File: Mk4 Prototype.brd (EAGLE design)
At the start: 6 parts

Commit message: Initial shape and some layout ideas
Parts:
- added ARTWORK1: ARTWORK_JOYSTICK, TiLDA Mk4 Parts:TILDA_ARTWORK_JOYSTICK
- added ARTWORK2: ARTWORK_KEYPAD, TiLDA Mk4 Parts:TILDA_ARTWORK_KEYPAD
- added C1: 0603 1u/10V/X5R, TiLDA Mk4 Parts:C0603K-SMALL
- added C38: 0603 4u7/10V/X5R, TiLDA Mk4 Parts:C0603K-SMALL
- added C45: 0603 100n/10V/X5R, TiLDA Mk4 Parts:C0603K-SMALL
- added IC1: MSP432E401, TiLDA Mk4 Parts:QFP128-0.4
- added IC2: AS4C8M16SA-7TCN, TiLDA Mk4 Parts:TSOP54-400
- added IC3: CC3120MOD, TiLDA Mk4 Parts:CC3100MOD-LWK
- added IC5: SIM800C, TiLDA Mk4 Parts:SIM800C
- added J2: ER-CON50HT-1, TiLDA Mk4 Parts:FH12-50S-0.5SH
- added J3: 2x5 1.27mm (NP), TiLDA Mk4 Parts:PINHEAD_2X05_127
- added JP1: (no value), TiLDA Mk4 Parts:JST-2-SMD
- added JP2: 1x03, TiLDA Mk4 Parts:1X03_LOCK
- added JP4: (NP), TiLDA Mk4 Parts:TC2030-MCP-NL
- added LAYERS1: LAYER_NUMBRS_4_SMALL, TiLDA Mk4 Parts:LAYER_NUMBERS_4_SMALL
- added LED1, LED2: (no value), TiLDA Mk4 Parts:WS2812B
- added OUTLINE1: TILDA_MK3_BOARDOUTLINE-MK4, TiLDA Mk4 Parts:TILDA_MK4_OUTLINE
- added Q8: CSD13202Q2, TiLDA Mk4 Parts:Q2
- added R44, R47, R48, R49: 0603 12R/5%, TiLDA Mk4 Parts:C0603K-SMALL
- added S1, S10, S11, S12, S13, S14, S15, S2, S3, S4, S5, S6, S7, S8, S9: SKPMAPE010, TiLDA Mk4 Parts:SKPMAPE010
- added S16, S17: 3X6X2.5, TiLDA Mk4 Parts:TACTILE_SWITCH_SMD_3X6X2.5H
- added S18: CUS-12TB, TiLDA Mk4 Parts:SWITCH-SPST-SMD-A
- added SW1: JOYSTICK, TiLDA Mk4 Parts:JOYSTICK_MULTICOMP_NOSILK
- added TP1, TP2, TP21, TP3, TP4: (NP), TiLDA Mk4 Parts:B1,27
- added U2: ER-TFT024-3 (NP), TiLDA Mk4 Parts:ER-TFT024-3
- FID1, FID2, FID3, FID4, FID5, FID6: device TiLDA Mk3 Parts:FIDUCIAL-1X2.5-STOP -> TiLDA Mk4 Parts:FIDUCIAL-1X2.5-STOP
- moved FID2 183.9 mm to (-62.0, 28.0), turned to 180 degrees
- moved FID5 183.9 mm to (-62.0, 28.0), turned to 180 degrees
- moved FID1 104.6 mm to (-12.0, 2.50), turned to 270 degrees
- moved FID6 104.6 mm to (-12.0, 2.50), turned to 270 degrees
- moved FID3 87.3 mm to (0.00, 80.0), turned to 180 degrees
- moved FID4 87.3 mm to (0.00, 80.0), turned to 180 degrees
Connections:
- new net 3V3: C38.2, C45.2, IC2.1, IC2.14, IC2.27, IC2.3, IC2.43, IC2.49, IC2.9, J2.1, J2.40, J2.41, J2.42, J3.1, JP4.1, OUTLINE1.3V3, SW1.COM
- new net ADC_X: J2.46
- new net ADC_Y: J2.47
- new net BTN_1: S1.2
- new net BTN_10: S10.2
- new net BTN_11: S11.2
- new net BTN_12: S12.2
- new net BTN_2: S2.2
- new net BTN_3: S3.2
- new net BTN_4: S4.2
- new net BTN_5: S5.2
- new net BTN_6: S6.2
- new net BTN_7: S7.2
- new net BTN_8: S8.2
- new net BTN_9: S9.2
- new net BTN_A: S13.2
- new net BTN_B: S15.2
- new net BTN_CALL: S16.2
- new net BTN_END: S17.2
- new net BTN_MENU: S14.2
- new net FSMC_A23: J2.37, TP4.TP
- new net GND: C1.2, C38.1, C45.1, IC1.114, IC1.17, IC1.48, IC1.55, IC1.58, IC1.80, IC2.12, IC2.28, IC2.41, IC2.46, IC2.52, IC2.54, IC2.6, IC3.1, IC3.16, IC3.2, IC3.27, IC3.28, IC3.30, IC3.32, IC3.38, IC3.43, IC3.55, IC3.56, IC3.57, IC3.58, IC3.59, IC3.60, IC3.61, IC3.62, IC3.63, IC5.13, IC5.19, IC5.21, IC5.27, IC5.30, IC5.31, IC5.33, IC5.36, IC5.37, IC5.8, J2.11, J2.12, J2.13, J2.14, J2.15, J2.16, J2.17, J2.18, J2.19, J2.20, J2.21, J2.22, J2.23, J2.24, J2.43, J2.48, J2.49, J2.50, J2.6, J3.3, J3.5, J3.9, JP1.1, JP2.1, JP4.5, LED1.3, LED2.3, OUTLINE1.GND, Q8.4, Q8.EP2, S1.1, S10.1, S11.1, S12.1, S13.1, S14.1, S15.1, S16.1, S17.1, S2.1, S3.1, S4.1, S5.1, S6.1, S7.1, S8.1, S9.1
- new net GNDA: IC1.10
- new net JOY_CEN: SW1.CTR
- new net JOY_DOWN: SW1.D
- new net JOY_LEFT: SW1.C
- new net JOY_RIGHT: SW1.B
- new net JOY_UP: SW1.A
- new net LCD0: J2.32, TP1.TP
- new net LCD1: J2.31
- new net LCD2: J2.30
- new net LCD3: J2.29
- new net LCD4: J2.28
- new net LCD5: J2.27
- new net LCD6: J2.26
- new net LCD7: J2.25
- new net LCD_!RST: J2.10
- new net LCD_CS: J2.38
- new net LCD_MODE: J2.7, J2.8, J2.9
- new net LCD_RD: J2.35, TP2.TP
- new net LCD_WRX: J2.36, TP3.TP
- new net LEDK1: J2.2, R47.2
- new net LEDK2: J2.3, R48.2
- new net LEDK3: J2.4, R49.2
- new net LEDK4: J2.5, R44.2
- new net N$64: Q8.1, Q8.2, Q8.5, Q8.6, Q8.EP1, R44.1, R47.1, R48.1, R49.1
- new net NRST: J3.10, JP4.3
- new net PA0: IC1.33
- new net PA1: IC1.34
- new net PA2: IC1.35
- new net PA3: IC1.36
- new net PA4: IC1.37
- new net PA5: IC1.38
- new net PB0: IC1.95
- new net PB1: IC1.96
- new net PB2: IC1.91
- new net PB4: IC1.121
- new net PB5: IC1.120
- new net PD0: IC1.1
- new net PD1: IC1.2
- new net PD2: IC1.3
- new net PD3: IC1.4
- new net PD4: IC1.125
- new net PD5: IC1.126
- new net PD6: IC1.127
- new net PD7: IC1.128
- new net PE0: IC1.15
- new net PE1: IC1.14
- new net PE2: IC1.13
- new net PE3: IC1.12
- new net PE4: IC1.123
- new net PE5: IC1.124
- new net PF0: IC1.42
- new net PF1: IC1.43
- new net PF2: IC1.44
- new net PF3: IC1.45
- new net PF4: IC1.46
- new net PJ0: IC1.116
- new net PJ1: IC1.117
- new net PK0: IC1.18
- new net PK1: IC1.19
- new net PK2: IC1.20
- new net PK3: IC1.21
- new net PK4: IC1.63
- new net PK6: IC1.61
- new net PK7: IC1.60
- new net PL4: IC1.85
- new net PL5: IC1.86
- new net PM4: IC1.74
- new net PM5: IC1.73
- new net PM6: IC1.72
- new net PM7: IC1.71
- new net PN0: IC1.107
- new net PN1: IC1.108
- new net PN2: IC1.109
- new net PN3: IC1.110
- new net PN4: IC1.111
- new net PN5: IC1.112
- new net PP0: IC1.118
- new net PP1: IC1.119
- new net PP4: IC1.105
- new net PP5: IC1.106
- new net PQ0: IC1.5
- new net PQ1: IC1.6
- new net PQ2: IC1.11
- new net PQ3: IC1.27
- new net PQ4: IC1.102
- new net REFA+: IC1.9
- new net SDRAM_!CAS: IC1.83, IC2.17
- new net SDRAM_!CS: IC1.103, IC2.19
- new net SDRAM_!RAS: IC1.84, IC2.18
- new net SDRAM_!WE: IC1.92, IC2.16
- new net SDRAM_A0: IC1.29, IC2.2, IC2.23
- new net SDRAM_A1: IC1.30, IC2.24, IC2.4
- new net SDRAM_A10: IC1.50, IC2.22, IC2.45
- new net SDRAM_A11: IC1.49, IC2.35, IC2.47
- new net SDRAM_A12: IC1.75, IC2.36, IC2.48
- new net SDRAM_A2: IC1.31, IC2.25, IC2.5
- new net SDRAM_A3: IC1.32, IC2.26, IC2.7
- new net SDRAM_A4: IC1.22, IC2.29, IC2.8
- new net SDRAM_A5: IC1.23, IC2.10, IC2.30
- new net SDRAM_A6: IC1.24, IC2.11, IC2.31
- new net SDRAM_A7: IC1.25, IC2.13, IC2.32
- new net SDRAM_A8: IC1.40, IC2.33, IC2.42
- new net SDRAM_A9: IC1.41, IC2.34, IC2.44
- new net SDRAM_BA0: IC1.76, IC2.20, IC2.50
- new net SDRAM_BA1: IC1.77, IC2.21, IC2.51
- new net SDRAM_CKE: IC1.104, IC2.37
- new net SDRAM_CLK: IC1.62, IC2.38
- new net SDRAM_D15: IC1.78, IC2.53
- new net SDRAM_DQMH: IC1.82, IC2.39
- new net SDRAM_DQML: IC1.81, IC2.15
- new net SIM_VDD: IC5.18
- new net SPI3_MISO: J2.33
- new net SPI3_MOSI: J2.34
- new net TCK_SWCLK: IC1.100, J3.4, JP4.4
- new net TDI: IC1.98
- new net TDO_SWO: IC1.97
- new net TEAR: J2.39, TP21.TP
- new net TIM17_CH1: Q8.3
- new net TMS_SWDIO: IC1.99, J3.2, JP4.2
- new net T_X: J2.44
- new net T_Y: J2.45
- new net USB_D_N: IC1.93
- new net USB_D_P: IC1.94
- new net USB_VBUS: IC5.24
- new net VBAT: IC1.68, IC5.34, IC5.35, JP1.2
- new net VBAT_1: IC3.37
- new net VBAT_2: IC3.40
- new net VDD: IC1.101, IC1.113, IC1.122, IC1.16, IC1.26, IC1.28, IC1.39, IC1.47, IC1.51, IC1.52, IC1.69, IC1.7, IC1.79, IC1.90
- new net VDDA: IC1.8
- new net VDDC: IC1.115, IC1.87
- new net VDD_EXT: IC5.40
- new net V_UNREG: C1.1, JP2.2, LED1.1, LED2.1
- new net WS2812: LED1.4
- new net WS2812_OUT: JP2.3, LED2.2
- new net WS28212_1: LED1.2, LED2.4
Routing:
- net SDRAM_A3: track 0.00 -> 32.2 mm
- net SDRAM_A2: track 0.00 -> 31.4 mm
- net SDRAM_A4: track 0.00 -> 31.4 mm
- net SDRAM_A5: track 0.00 -> 30.5 mm
- net SDRAM_A1: track 0.00 -> 30.4 mm
- net SDRAM_A0: track 0.00 -> 30.3 mm
- net SDRAM_A10: track 0.00 -> 29.9 mm, vias 0 -> 2
- net SDRAM_BA1: track 0.00 -> 29.5 mm, vias 0 -> 2
- net SDRAM_A6: track 0.00 -> 29.4 mm
- net SDRAM_A7: track 0.00 -> 28.4 mm
- net SDRAM_BA0: track 0.00 -> 28.0 mm, vias 0 -> 2
- net SDRAM_A8: track 0.00 -> 25.4 mm
- net SDRAM_A9: track 0.00 -> 24.6 mm
- net SDRAM_A11: track 0.00 -> 22.8 mm
- net SDRAM_A12: track 0.00 -> 21.9 mm
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- added copper zone on layer 2, net 3V3
- added copper zone on layer 15, net GND
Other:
- board outline added: 124.4 x 80 mm

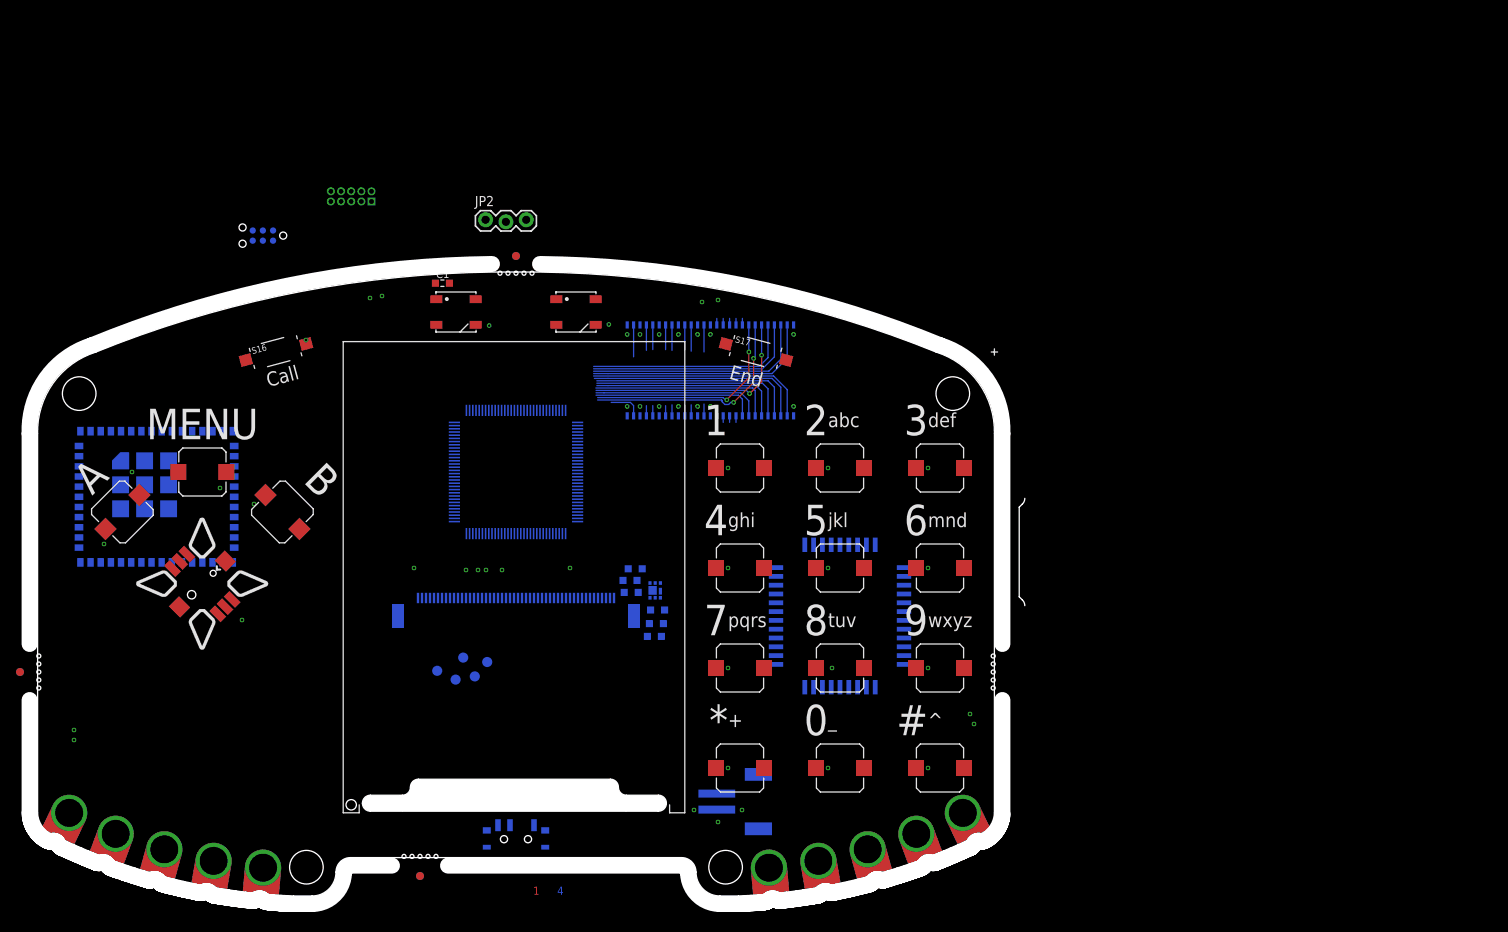
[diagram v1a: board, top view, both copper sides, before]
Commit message: Drop in a few more parts and identified some options for Spk, MIC and antennas
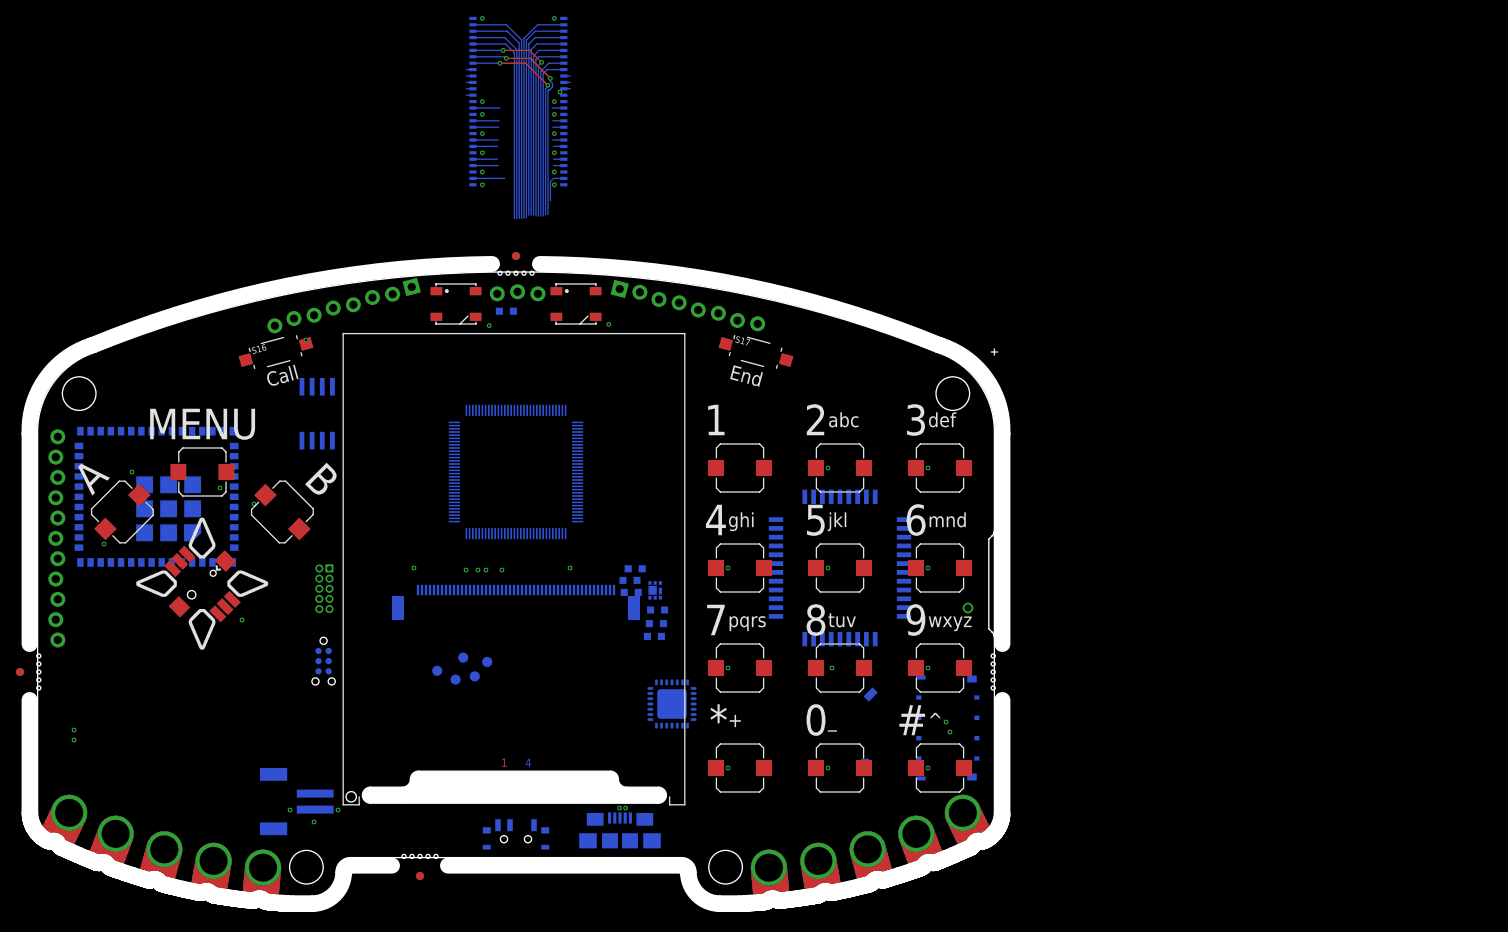
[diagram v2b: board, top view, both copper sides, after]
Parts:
- added IC4: MCP23017ML, TiLDA Mk4 Parts:QFN28-ML_6X6MM
- added IC6: SST26VF064B-104I/SM, TiLDA Mk4 Parts:SO08-EIAJ
- added J1: 78723-1001, TiLDA Mk4 Parts:MSIM-MOLEX-LWK
- added J4: ANTENNA-GSM, TiLDA Mk4 Parts:GSM-ANTENNA
- added JP3: 1x11, TiLDA Mk4 Parts:1X11_LOCK
- added JP5, JP6: 1x08, TiLDA Mk4 Parts:1X08_LOCK
- added U1: (no value), TiLDA Mk4 Parts:USB-AB-MICRO-SMD_LWK
- moved JP1 57.6 mm to (-28.8, 11.8), turned to 270 degrees
- moved JP4 50.9 mm to (-24.1, 31.9), turned to 270 degrees
- moved J3 49.2 mm to (-23.9, 38.4), turned to 270 degrees
- moved IC2 41.3 mm to (0.30, 99.3), turned to 90 degrees
- moved LAYERS1 16.5 mm to (-2.00, 16.0)
- moved JP2 9.12 mm to (-2.34, 75.4), flipped to the bottom, turned to 180 degrees
- moved C1 8.73 mm to (-1.20, 73.1), flipped to the bottom
- moved IC5 6.00 mm to (40.5, 41.0)
- moved J2 1.00 mm to (0.00, 35.0)
- moved LED1 1.00 mm to (-7.50, 74.0)
- moved LED2 1.00 mm to (7.50, 74.0)
- moved U2 1.00 mm to (0.00, 35.0)
- turned IC3 to 0 degrees
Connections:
- new net BT_ANT: IC5.20
- new net GSM_ANT: IC5.32, J4.ANT
- new net N$36: IC3.31
- new net VCC: J1.C1
- new net VSS: IC4.6
- net GND: now also J1.C4, J1.C5, J1.GND1, J1.GND2, J1.GND3, J1.GND4, J1.GND5, J1.GND6
- net TDI: now also J3.8
- net TDO_SWO: now also J3.6, JP4.6
- net VDD: now also IC4.5
- net V_UNREG: now also OUTLINE1.VBATT
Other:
- board size 124.4 x 80 mm -> 121.6 x 80 mm
- board text added: "GND"

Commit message: NIght 2
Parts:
- removed JP3: 1x11, TiLDA Mk4 Parts:1X11_LOCK
- removed TP2, TP21, TP3, TP4: (NP), TiLDA Mk4 Parts:B1,27
- added C10, C11, C12, C13, C15, C2, C21, C22, C23, C24, C25, C26, C27, C28, C3, C4, C5, C8, C9: 0402/100n/10V/X5R, TiLDA Mk4 Parts:C0402-SMALLER
- added C14, C7: 0603/1u/10V/X5R, TiLDA Mk4 Parts:C0603K-SMALL
- added C16, C17, C18, C19: 0402/12p/50V/C0G, TiLDA Mk4 Parts:C0402-SMALLER
- added C20: 0603/3300p/50V/X7R, TiLDA Mk4 Parts:C0603K-SMALL
- added C6: 0603/2u2/10V/X5R, TiLDA Mk4 Parts:C0603K-SMALL
- added IC7: TPD3E001DRL, TiLDA Mk4 Parts:DRL-5
- added JP7: 1x14, TiLDA Mk4 Parts:1X14_LOCK
- added L2: BLM18KG121TN1D, TiLDA Mk4 Parts:WUERTH-0805
- added LED3: 0603 RED, TiLDA Mk4 Parts:LED-0603-CORRECT
- added LED4: 0603 GREEN, TiLDA Mk4 Parts:LED-0603-CORRECT
- added LED5: (no value), TiLDA Mk4 Parts:LED5MM
- added Q3: CSD13202Q2, TiLDA Mk3 Parts:Q2
- added R1, R2: 0402/1K/5%, TiLDA Mk4 Parts:R0402-SMALLER
- added R10, R9: 0402/10k/5%, TiLDA Mk4 Parts:R0402-SMALLER
- added R11: (no value), TiLDA Mk4 Parts:0309/10
- added R12: 0402/2k/5%, TiLDA Mk4 Parts:R0402-SMALLER
- added R14: 0402/4k7/5%, TiLDA Mk4 Parts:R0402-SMALLER
- added R3: 0402/4k87/5%, TiLDA Mk4 Parts:R0402-SMALLER
- added R4: 0402/10K/5%, TiLDA Mk4 Parts:R0402-SMALLER
- added R5, R7: 0402/1M/5%, TiLDA Mk4 Parts:R0402-SMALLER
- added R6: 0402/2K/5%, TiLDA Mk4 Parts:R0402-SMALLER
- added R8: 0402/100/5%, TiLDA Mk4 Parts:R0402-SMALLER
- added S19, S20: 3X6X2.5, TiLDA Mk4 Parts:TACTILE_SWITCH_SMD_3X6X2.5H
- added X1: FC-135R 32.768KHZ 9PF, TiLDA Mk4 Parts:RESONATOR_EPSON_FC_145
- added X2: NX3225GA-25.000M-STD-CRG-2, TiLDA Mk4 Parts:CRYSTAL-3.2-2.5
- C1: value 0603 1u/10V/X5R -> 0603/1u/10V/X5R
- C38: value 0603 4u7/10V/X5R -> 0603/4u7/10V/X5R
- C45: value 0603 100n/10V/X5R -> 0402/100n/10V/X5R; device TiLDA Mk4 Parts:C0603K-SMALL -> TiLDA Mk4 Parts:C0402-SMALLER
- R44, R47, R48, R49: value 0603 12R/5% -> 0402/12R/5%; device TiLDA Mk4 Parts:C0603K-SMALL -> TiLDA Mk4 Parts:R0402-SMALLER
- TP1: value (NP) -> TP
- moved U1 68.6 mm to (10.4, 75.5), turned to 274 degrees
- moved J3 57.8 mm to (29.9, 59.5), turned to 0 degrees
- moved JP1 57.7 mm to (28.8, 15.8), turned to 90 degrees
- moved JP4 54.4 mm to (24.3, 56.9), turned to 90 degrees
- moved IC2 51.6 mm to (-21.8, 52.7), turned to 270 degrees
- moved IC6 41.7 mm to (13.2, 43.1), turned to 270 degrees
- moved TP1 31.7 mm to (-7.60, 60.7), turned to 0 degrees
- moved C38 26.5 mm to (-8.25, 40.2)
- moved C45 26.2 mm to (-8.25, 39.0)
- moved R49 9.44 mm to (10.5, 39.0), turned to 270 degrees
- moved C1 6.95 mm to (-7.60, 75.8), turned to 270 degrees
- moved JP5 5.10 mm to (18.0, 75.0)
- moved JP6 5.10 mm to (-18.0, 75.0)
- moved R44 5.01 mm to (9.50, 39.0), turned to 270 degrees
- moved R48 3.89 mm to (11.5, 39.0), turned to 270 degrees
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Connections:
- net PP1 renamed SSI3DAT3
- removed net FSMC_A23: J2.37, TP4.TP
- removed net GNDA: IC1.10
- removed net LCD0: J2.32, TP1.TP
- removed net LCD1: J2.31
- removed net LCD2: J2.30
- removed net LCD3: J2.29
- removed net LCD4: J2.28
- removed net LCD5: J2.27
- removed net LCD6: J2.26
- removed net LCD7: J2.25
- removed net LCD_MODE: J2.7, J2.8, J2.9
- removed net LCD_RD: J2.35, TP2.TP
- removed net LCD_WRX: J2.36, TP3.TP
- removed net PA2: IC1.35
- removed net PA3: IC1.36
- removed net PA4: IC1.37
- removed net PA5: IC1.38
- removed net PB0: IC1.95
- removed net PB1: IC1.96
- removed net PF0: IC1.42
- removed net PF4: IC1.46
- removed net PK1: IC1.19
- removed net PK2: IC1.20
- removed net PK3: IC1.21
- removed net PK4: IC1.63
- removed net PK6: IC1.61
- removed net PM4: IC1.74
- removed net PM5: IC1.73
- removed net PM7: IC1.71
- removed net PN0: IC1.107
- removed net PP0: IC1.118
- removed net PQ0: IC1.5
- removed net PQ1: IC1.6
- removed net PQ2: IC1.11
- removed net PQ3: IC1.27
- removed net REFA+: IC1.9
- removed net SPI3_MISO: J2.33
- removed net SPI3_MOSI: J2.34
- removed net TEAR: J2.39, TP21.TP
- removed net TIM17_CH1: Q8.3
- removed net VDD: IC1.101, IC1.113, IC1.122, IC1.16, IC1.26, IC1.28, IC1.39, IC1.47, IC1.51, IC1.52, IC1.69, IC1.7, IC1.79, IC1.90, IC4.5
- removed net VDDA: IC1.8
- removed net VSS: IC4.6
- new net !CC_HIB: IC3.4
- new net !CC_RST: IC3.35
- new net !HIB: IC1.65, TP1.TP
- new net !RESET: C15.2, IC1.70, J3.10, R4.1, S19.2
- new net !WAKE: IC1.64, R5.1, S20.2
- new net 3V3_POE: C5.2, JP7.14
- new net CC_IRQ: IC3.11
- new net CH1: OUTLINE1.CH4
- new net CH2: OUTLINE1.CH3
- new net CH3: OUTLINE1.CH2
- new net CH4: OUTLINE1.CH1
- new net EN0RXI_N: IC1.53, JP7.13
- new net EN0RXI_P: IC1.54, JP7.11
- new net EN0TXO_N: IC1.56, JP7.7
- new net EN0TXO_P: IC1.57, JP7.6
- new net ETHLED0: IC1.63, R1.2
- new net ETHLED1: IC1.61, R2.2
- new net FET: Q3.3
- new net FET_OUT: LED5.K, OUTLINE1.FET, Q3.1, Q3.2, Q3.5, Q3.6, Q3.EP1
- new net I2C2_SCL: OUTLINE1.SCL
- new net I2C2_SDA: OUTLINE1.SDA
- new net I2C_SCL: IC4.8
- new net I2C_SDA: IC4.9
- new net LCD_BLIGHT: IC1.42, Q8.3
- new net LCD_CLK: IC1.35, J2.37
- new net LCD_DCX: IC1.20, J2.36
- new net LCD_MISO: IC1.38, J2.33
- new net LCD_MOSI: IC1.37, J2.34
- new net LCD_TEAR: IC1.19, J2.39
- new net LED1: IC1.95, R12.2
- new net LED2: IC1.96, R14.2
- new net MCP_INT: IC4.16
- new net N$1: LED5.A, R11.1
- new net N$3: JP7.3, R1.1
- new net N$4: JP7.5, R2.1
- new net N$5: IC1.59, R3.1
- new net N$51: LED4.A, R14.1
- new net N$52: LED3.A, R12.1
- new net N$6: C20.2, R7.1, U1.SHIELD, U1.SHIELD@0, U1.SHIELD@1, U1.SHIELD@2, U1.SHIELD@3, U1.SHIELD@5
- new net OSC0: C16.2, IC1.88, X2.1
- new net OSC1: IC1.89, R6.1
- new net OSC1_R: C17.2, R6.2, X2.3
- new net SPI1_MISO: IC3.7
- new net SPI1_MOSI: IC3.6
- new net SPI1_NSS: IC3.8
- new net SPI1_SCK: IC3.5
- new net SSI3_CLK: IC1.5, IC6.6
- new net SSI3_DAT0: IC1.11, IC6.5
- new net SSI3_DAT1: IC1.27, IC6.2
- new net SSI3_DAT2: IC1.46, IC6.3, R10.2
- new net SSI3_DAT3: IC6.7, R9.2
- new net SSI3_FSS: IC1.6, IC6.1
- new net USART1_RX: IC3.46
- new net USART1_TX: IC3.47
- new net USB_ID: R8.2
- new net USB_ID_R: IC7.4, R8.1, U1.ID
- new net VBUS: IC7.5, L2.2
- new net VBUS_L: L2.1, U1.VBUS
- new net XOSC0: C18.2, IC1.66, X1.P$1
- new net XOSC1: C19.2, IC1.67, X1.P$2
- net 3V3: now also C10.2, C11.2, C12.2, C13.2, C14.2, C2.2, C21.2, C22.2, C23.2, C24.2, C25.2, C26.2, C27.2, C28.2, C3.2, C4.2, C9.2, IC1.101, IC1.113, IC1.122, IC1.16, IC1.26, IC1.28, IC1.39, IC1.47, IC1.51, IC1.52, IC1.68, IC1.69, IC1.7, IC1.79, IC1.8, IC1.9, IC1.90, IC4.5, IC6.8, J2.35, J2.7, J2.8, J2.9, JP7.12, JP7.8, R10.1, R11.2, R4.2, R5.2, R9.1
- net BTN_1: now also IC4.17
- net BTN_10: now also IC4.26
- net BTN_11: now also IC4.27
- net BTN_12: now also IC4.28
- net BTN_2: now also IC4.18
- net BTN_3: now also IC4.19
- net BTN_4: now also IC4.20
- net BTN_5: now also IC4.21
- net BTN_6: now also IC4.22
- net BTN_7: now also IC4.23
- net BTN_8: now also IC4.24
- net BTN_9: now also IC4.25
- net BTN_A: now also IC4.3
- net BTN_B: now also IC4.4
- net BTN_CALL: now also IC4.1
- net BTN_END: now also IC4.2
- net GND: now also C10.1, C11.1, C12.1, C13.1, C14.1, C15.1, C16.1, C17.1, C18.1, C19.1, C2.1, C20.1, C21.1, C22.1, C23.1, C24.1, C25.1, C26.1, C27.1, C28.1, C3.1, C4.1, C5.1, C6.1, C7.1, C8.1, C9.1, IC1.10, IC4.11, IC4.12, IC4.13, IC4.6, IC6.4, IC7.3, J2.25, J2.26, J2.27, J2.28, J2.29, J2.30, J2.31, J2.32, JP5.1, JP6.1, JP7.1, JP7.2, JP7.4, LED3.C, LED4.C, Q3.4, Q3.EP2, R3.2, R7.2, S19.1, S20.1, U1.GND, X2.2, X2.4
- net JOY_CEN: now also IC1.118
- net JOY_DOWN: now also IC1.107
- net JOY_LEFT: now also IC1.73
- net JOY_RIGHT: now also IC1.74
- net JOY_UP: now also IC1.71
- net LCD_!RST: now also IC1.21
- net LCD_CS: now also IC1.36
- net NRST: no longer J3.10
- net USB_D_N: now also IC7.1, U1.D-
- net USB_D_P: now also IC7.2, U1.D+
- net VBAT: no longer IC1.68
- net VDDC: now also C6.2, C7.2, C8.2
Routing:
- net GND: track 0.00 -> 63.1 mm, vias 34 -> 70
- net 3V3: track 0.00 -> 33.1 mm, vias 13 -> 32
- net SDRAM_A3: track 32.2 -> 0.00 mm
- net SDRAM_A2: track 31.4 -> 0.00 mm
- net SDRAM_A4: track 31.4 -> 0.00 mm
- net SDRAM_A5: track 30.5 -> 0.00 mm
- net SDRAM_A1: track 30.4 -> 0.00 mm
- net SDRAM_A0: track 30.3 -> 0.00 mm
- net SDRAM_A10: track 29.9 -> 0.00 mm, vias 2 -> 0
- net SDRAM_BA1: track 29.5 -> 0.00 mm, vias 2 -> 0
- net SDRAM_A6: track 29.4 -> 0.00 mm
- net SDRAM_A7: track 28.4 -> 0.00 mm
- net SDRAM_BA0: track 28.0 -> 0.00 mm, vias 2 -> 0
- net SDRAM_A8: track 25.4 -> 0.00 mm
- net SDRAM_A9: track 24.6 -> 0.00 mm
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- added copper zone on layer 16, net GND
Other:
- board text added: "!HIB"
- board text added: "0V"
- board text added: "3.3V"
- board text added: "CH1"
- board text added: "CH2"
- board text added: "CH3"
- board text added: "CH4"
- board text added: "FET"
- board text added: "GPIO?"
- board text added: "I2C?"
- board text added: "OFF"
- board text added: "ON"
- board text added: "Reset"
- board text added: "SCL"
- board text added: "SDA"
- board text added: "TIM2"
- board text added: "VBATT"
- board text added: "Wake"
